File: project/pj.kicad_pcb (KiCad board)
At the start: 2 copper layers, 65 x 56.5 mm, 18 parts, among them J1 RPi_GPIO, J10 Pi PWR enable, J12 Conn_01x16_Pin, J2 2B+, J3 zero, J4 3A+, J5 3B+, J6 Pi 4, J7 Reset Pico, J8 Reset Pi, J9 Pi External PWR, SW1 Reset Pi, SW2 Reset Pico

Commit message: spi sch
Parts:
- moved J3 45.8 mm to (90.6, 48.4)
- moved J4 2.43 mm to (96.7, 52.0)
- moved J1 0.06 mm to (69.0, 44.5)
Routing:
- net Net-(A1-GPIO19): track 177.9 -> 162.9 mm
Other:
- board text added: "github.com/CarlFK/pj v1.1"
- board text removed: "github.com/CarlFK/pj v1.0"
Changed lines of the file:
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@@
 		(pad_to_mask_clearance 0)
 		(allow_soldermask_bridges_in_footprints no)
+		(grid_origin 93.15 45.89)
 		(pcbplotparams
 			(layerselection 0x00010fc_ffffffff)
@@
 		(fp_arc
 			(start 10.579676 25.189937)
-			(mid 10.357958 25.493991)
+			(mid 10.357946 25.493957)
 			(end 10 25.61)
 			(stroke
@@
 	(footprint "RPI_Hat:RPI_Hat_B+"
 		(layer "F.Cu")
-		(at 68.92 44.495)
+		(at 68.97 44.522)
 		(property "Reference" "J1"
 			(at 12.6 3.545 0)
@@
 			(layer "Dwgs.User")
 			(pts
-				(xy 41.42 60.495) (xy 36.42 60.495)
+				(xy 41.47 60.522) (xy 36.47 60.522)
 			)
 			(height 2)
-			(gr_text "5.0000 mm"
-				(at 38.92 56.845 0)
+			(gr_text "196.8504 mils"
+				(at 38.97 56.872 0)
 				(layer "Dwgs.User")
 				(effects
@@
 			(layer "Dwgs.User")
 			(pts
-				(xy 83.42 93.995) (xy 83.42 76.995)
+				(xy 83.47 94.022) (xy 83.47 77.022)
 			)
 			(height 3)
-			(gr_text "17.0000 mm"
-				(at 84.77 85.495 90)
+			(gr_text "669.2913 mils"
+				(at 84.82 85.522 90)
 				(layer "Dwgs.User")
 				(effects
@@
 			(layer "Dwgs.User")
 			(pts
-				(xy 68.92 46.495001) (xy 39.92 46.495001)
+				(xy 68.97 46.522001) (xy 39.97 46.522001)
 			)
 			(height -2.499999)
-			(gr_text "29.0000 mm"
-				(at 54.42 50.995001 0)
+			(gr_text "1141.7323 mils"
+				(at 54.47 51.022001 0)
 				(layer "Dwgs.User")
 				(effects
@@
 			(layer "Dwgs.User")
 			(pts
-				(xy 35.42 96.995) (xy 35.42 77.495)
+				(xy 35.47 97.022) (xy 35.47 77.522)
 			)
 			(height -3)
-			(gr_text "19.5000 mm"
-				(at 30.77 87.245 90)
+			(gr_text "767.7165 mils"
+				(at 30.82 87.272 90)
 				(layer "Dwgs.User")
 				(effects
@@
 			(layer "Dwgs.User")
 			(pts
-				(xy 102.42 93.495) (xy 102.42 44.495)
+				(xy 102.47 93.522) (xy 102.47 44.522)
 			)
 			(height 2.999999)
-			(gr_text "49.0000 mm"
-				(at 103.769999 68.995 90)
+			(gr_text "1929.1339 mils"
+				(at 103.819999 69.022 90)
 				(layer "Dwgs.User")
 				(effects
@@
 			(layer "Dwgs.User")
 			(pts
-				(xy 102.42 96.995) (xy 102.42 40.995)
+				(xy 102.47 97.022) (xy 102.47 41.022)
 			)
 			(height 8)
-			(gr_text "56.0000 mm"
-				(at 108.77 68.995 90)
+			(gr_text "2204.7244 mils"
+				(at 108.82 69.022 90)
 				(layer "Dwgs.User")
 				(effects
@@
 			(layer "Dwgs.User")
 			(pts
-				(xy 101.42 39.495) (xy 36.42 39.495)
+				(xy 101.47 39.522) (xy 36.47 39.522)
 			)
 			(height 7)
-			(gr_text "65.0000 mm"
-				(at 68.92 30.845 0)
+			(gr_text "2559.0551 mils"
+				(at 68.97 30.872 0)
 				(layer "Dwgs.User")
 				(effects
@@
 			(layer "Dwgs.User")
 			(pts
-				(xy 82.42 75.995) (xy 80.42 75.995)
+				(xy 82.47 76.022) (xy 80.47 76.022)
 			)
 			(height 2.499999)
-			(gr_text "2.0000 mm"
-				(at 81.42 71.845001 0)
+			(gr_text "78.7402 mils"
+				(at 81.47 71.872001 0)
 				(layer "Dwgs.User")
 				(effects
@@
 			(layer "Dwgs.User")
 			(pts
-				(xy 42.42 77.495) (xy 42.42 60.495)
+				(xy 42.47 77.522) (xy 42.47 60.522)
 			)
 			(height 2)
-			(gr_text "17.0000 mm"
-				(at 42.77 68.995 90)
+			(gr_text "669.2913 mils"
+				(at 42.82 69.022 90)
 				(layer "Dwgs.User")
 				(effects
@@
 			(layer "Dwgs.User")
 			(pts
-				(xy 102.42 96.995) (xy 102.42 40.495)
+				(xy 102.47 97.022) (xy 102.47 40.522)
 			)
 			(height 12)
-			(gr_text "56.5000 mm"
-				(at 112.77 68.745 90)
+			(gr_text "2224.4094 mils"
+				(at 112.82 68.772 90)
 				(layer "Dwgs.User")
 				(effects
@@
 			(layer "Dwgs.User")
 			(pts
-				(xy 97.92 39.495) (xy 39.92 39.495)
+				(xy 97.97 39.522) (xy 39.97 39.522)
 			)
 			(height 2.5)
-			(gr_text "58.0000 mm"
-				(at 68.92 35.345 0)
+			(gr_text "2283.4646 mils"
+				(at 68.97 35.372 0)
 				(layer "Dwgs.User")
 				(effects
@@
 			(layer "Dwgs.User")
 			(pts
-				(xy 79.42 96.995) (xy 79.42 85.495)
+				(xy 79.47 97.022) (xy 79.47 85.522)
 			)
 			(height -2.499999)
-			(gr_text "11.5000 mm"
-				(at 75.270001 91.245 90)
+			(gr_text "452.7559 mils"
+				(at 75.320001 91.272 90)
 				(layer "Dwgs.User")
 				(effects
@@
 			(layer "Dwgs.User")
 			(pts
-				(xy 39.92 97.995) (xy 36.42 97.995)
+				(xy 39.97 98.022) (xy 36.47 98.022)
 			)
 			(height -2.5)
-			(gr_text "3.5000 mm"
-				(at 38.17 98.845 0)
+			(gr_text "137.7953 mils"
+				(at 38.22 98.872 0)
 				(layer "Dwgs.User")
 				(effects
@@
 			(layer "Dwgs.User")
 			(pts
-				(xy 43.42 96.995) (xy 43.42 93.495)
+				(xy 43.47 97.022) (xy 43.47 93.522)
 			)
 			(height 3)
-			(gr_text "3.5000 mm"
-				(at 44.77 95.245 90)
+			(gr_text "137.7953 mils"
+				(at 44.82 95.272 90)
 				(layer "Dwgs.User")
 				(effects
@@
 	(footprint "Connector_PinSocket_2.54mm:PinSocket_1x02_P2.54mm_Vertical"
 		(layer "B.Cu")
-		(at 44.82 48.37 -90)
+		(at 90.61 48.43 -90)
 		(descr "Through hole straight socket strip, 1x02, 2.54mm pitch, single row (from Kicad 4.0.7), script generated")
 		(tags "Through hole socket strip THT 1x02 2.54mm single row")
@@
 		)
 		(property "Value" "zero"
-			(at 0.76 2.76 0)
+			(at 0 -5.08 0)
 			(layer "F.SilkS")
 			(effects
@@
 	(footprint "Connector_PinSocket_2.54mm:PinSocket_1x02_P2.54mm_Vertical"
 		(layer "B.Cu")
-		(at 96.69 49.61 -90)
+		(at 96.72 52.04 -90)
 		(descr "Through hole straight socket strip, 1x02, 2.54mm pitch, single row (from Kicad 4.0.7), script generated")
 		(tags "Through hole socket strip THT 1x02 2.54mm single row")
@@
 		)
 		(property "Value" "3A+"
-			(at 2.09 -0.41 180)
+			(at -1.86 -0.19 180)
 			(layer "F.SilkS")
 			(effects
@@
 		)
 	)
-	(gr_text "github.com/CarlFK/pj v1.0"
+	(gr_text "github.com/CarlFK/pj v1.1"
+		(locked yes)
 		(at 97.55 59.4 270)
 		(layer "F.SilkS")
@@
 	)
 	(segment
-		(start 41.23 54.26)
-		(end 41.23 55.92)
+		(start 99.21 57.08)
+		(end 99.22 57.09)
 		(width 0.2)
 		(layer "F.Cu")
@@
 	)
 	(segment
-		(start 39.92 49.06)
-		(end 39.92 52.95)
-		(width 0.2)
-		(layer "F.Cu")
-		(net 13)
-	)
-	(segment
-		(start 44.82 48.37)
-		(end 40.61 48.37)
-		(width 0.2)
-		(layer "F.Cu")
-		(net 13)
-	)
-	(segment
-		(start 96.69 52.13)
-		(end 99.22 54.66)
+		(start 96.72 52.04)
+		(end 96.72 53.26)
 		(width 0.2)
 		(layer "F.Cu")
@@
 	)
 	(segment
-		(start 40.61 48.37)
-		(end 39.92 49.06)
-		(width 0.2)
-		(layer "F.Cu")
-		(net 13)
-	)
-	(segment
 		(start 99.22 57.09)
 		(end 99.22 67.51)
@@
 	)
 	(segment
-		(start 99.22 57.09)
-		(end 99.22 54.66)
+		(start 48.32 80.83)
+		(end 46 78.51)
 		(width 0.2)
 		(layer "F.Cu")
@@
 	)
 	(segment
-		(start 48.32 80.83)
-		(end 46 78.51)
+		(start 96.72 53.26)
+		(end 99.21 55.75)
 		(width 0.2)
 		(layer "F.Cu")
@@
 	)
 	(segment
+		(start 99.21 55.75)
+		(end 99.21 57.08)
+		(width 0.2)
+		(layer "F.Cu")
+		(net 13)
+	)
+	(segment
 		(start 54.91 71.3425)
 		(end 54.8475 71.28)
@@
 	)
 	(segment
-		(start 39.92 52.95)
-		(end 41.23 54.26)
-		(width 0.2)
-		(layer "F.Cu")
-		(net 13)
-	)
-	(segment
 		(start 44.075 76.585)
 		(end 46 78.51)
@@
 		(width 0.2)
 		(layer "F.Cu")
-		(net 13)
-	)
-	(segment
-		(start 96.69 49.61)
-		(end 96.69 52.13)
-		(width 0.2)
-		(layer "F.Cu")

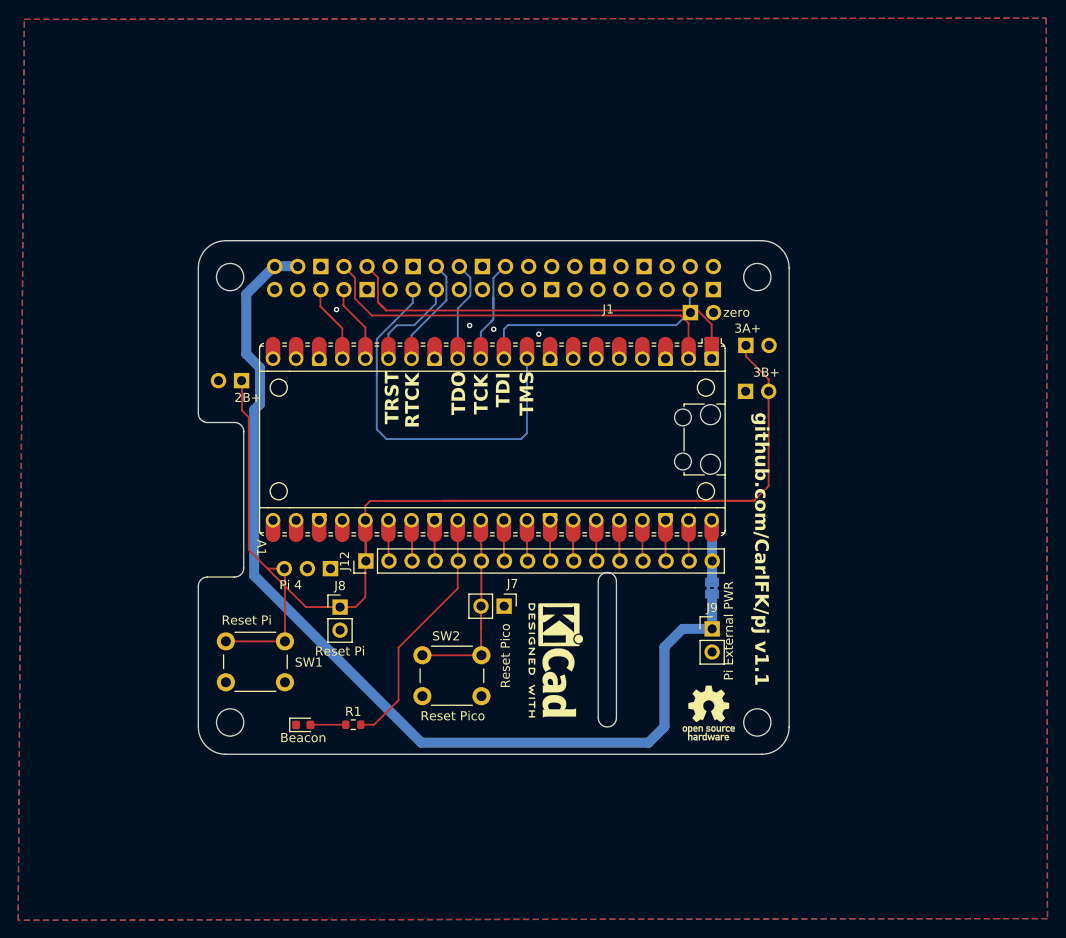
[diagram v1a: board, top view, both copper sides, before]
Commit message: add spi symbol
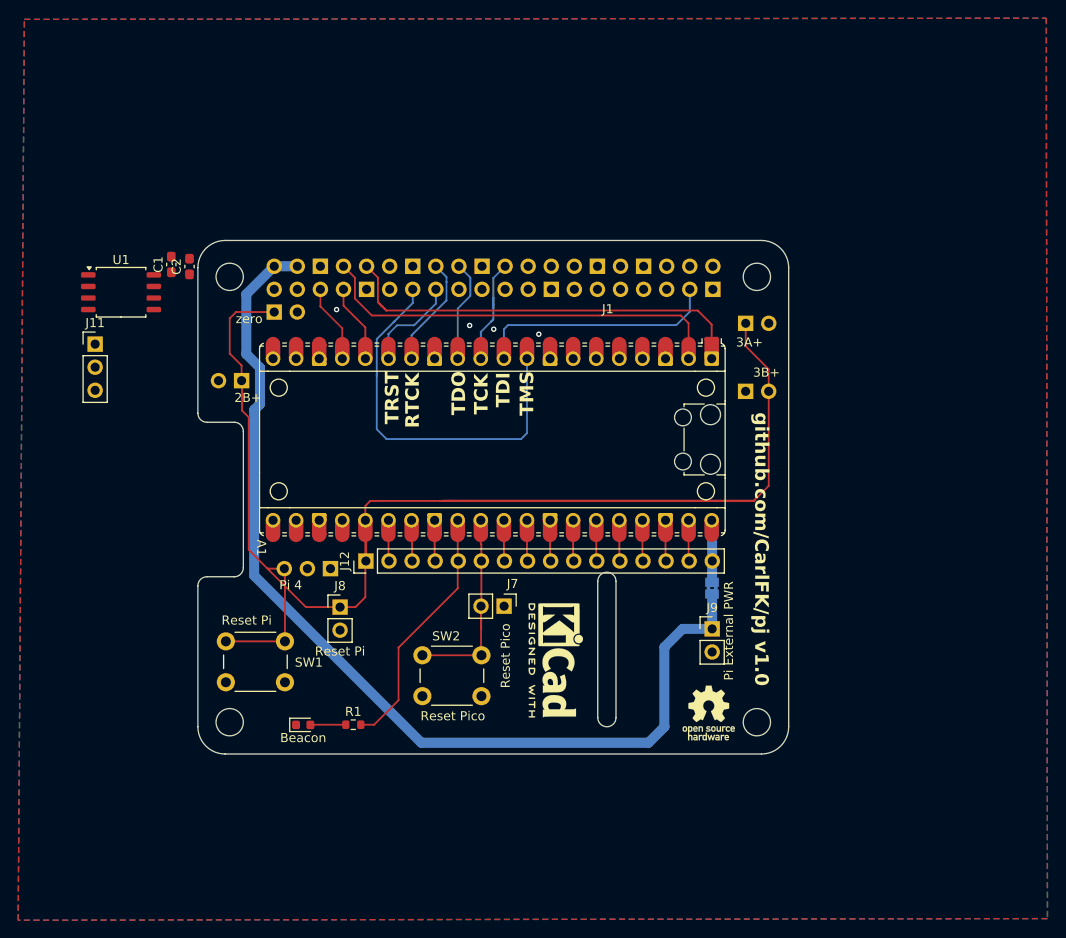
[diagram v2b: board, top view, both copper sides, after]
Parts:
- added C1: .1, Capacitor_SMD:C_0603_1608Metric_Pad1.08x0.95mm_HandSolder, F.Cu at (33.5, 43.1)
- added C2: 1, Capacitor_SMD:C_0603_1608Metric_Pad1.08x0.95mm_HandSolder, F.Cu at (35.5, 43.4)
- added J11: Conn_01x03_Pin, Connector_PinHeader_2.54mm:PinHeader_1x03_P2.54mm_Vertical, F.Cu at (25.1, 51.9)
- added U1: W25Q32JVSS, Package_SO:SOIC-8_5.23x5.23mm_P1.27mm, F.Cu at (28.0, 46.2)
- moved J3 45.8 mm to (44.8, 48.4)
- moved J4 2.43 mm to (96.7, 49.6)
- moved J1 0.06 mm to (68.9, 44.5)
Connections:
- net Net-(A1-3V3) renamed +3.3V
- net Net-(A1-GPIO19) renamed /reset pi
- net Net-(A1-VBUS) renamed /pi power
- A1 pad 19: unconnected-(A1-GPIO14-Pad19) -> /RPI_SPI_CE0
- A1 pad 20: unconnected-(A1-GPIO15-Pad20) -> /RPI_SPI_CE1
- A1 pad 4: unconnected-(A1-GPIO2-Pad4) -> /RPI_SPI_CLK
- A1 pad 5: unconnected-(A1-GPIO3-Pad5) -> /RPI_SPI_MISO
- A1 pad 6: unconnected-(A1-GPIO4-Pad6) -> /RPI_SPI_MOSI
- J1 pad 19: unconnected-(J1-BCM10_MOSI-Pad19) -> /RPI_SPI_MOSI
- J1 pad 21: unconnected-(J1-BCM9_MISO-Pad21) -> /RPI_SPI_MISO
- J1 pad 23: unconnected-(J1-BCM11_SCLK-Pad23) -> /RPI_SPI_CLK
- J1 pad 24: unconnected-(J1-BCM8_CE0-Pad24) -> /RPI_SPI_CE0
- J1 pad 26: unconnected-(J1-BCM7_CE1-Pad26) -> /RPI_SPI_CE1
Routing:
- net /reset pi: track 162.9 -> 177.9 mm
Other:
- board text added: "github.com/CarlFK/pj v1.0"
- board text removed: "github.com/CarlFK/pj v1.1"

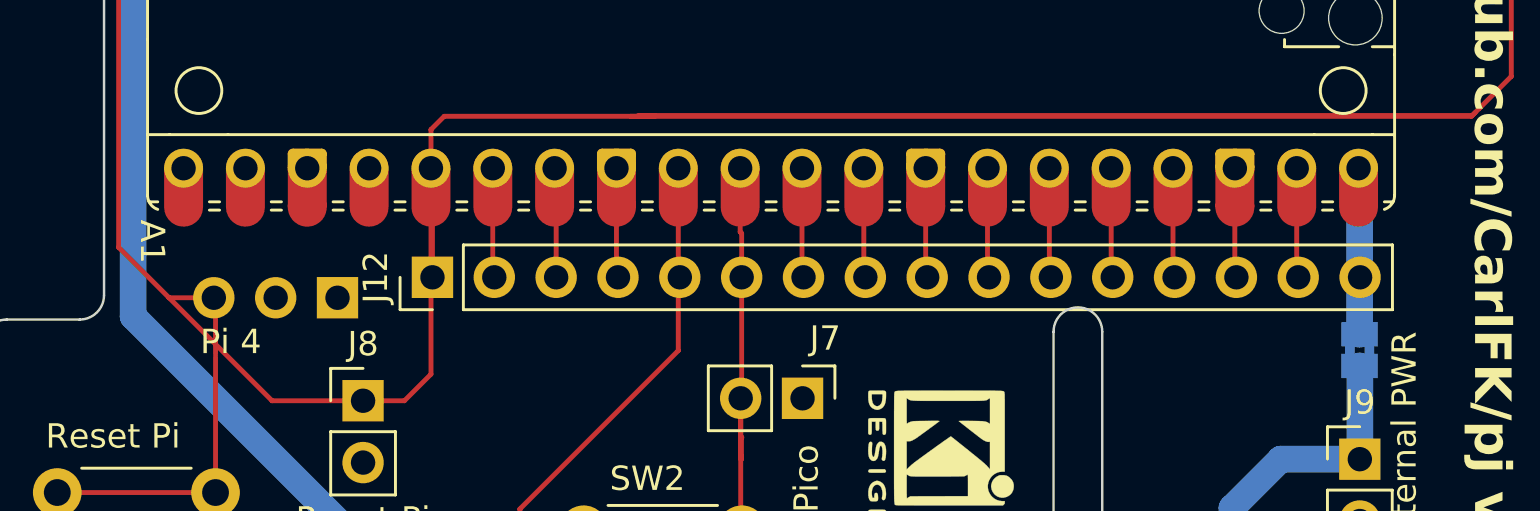
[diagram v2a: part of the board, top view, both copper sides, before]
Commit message: removing debug header
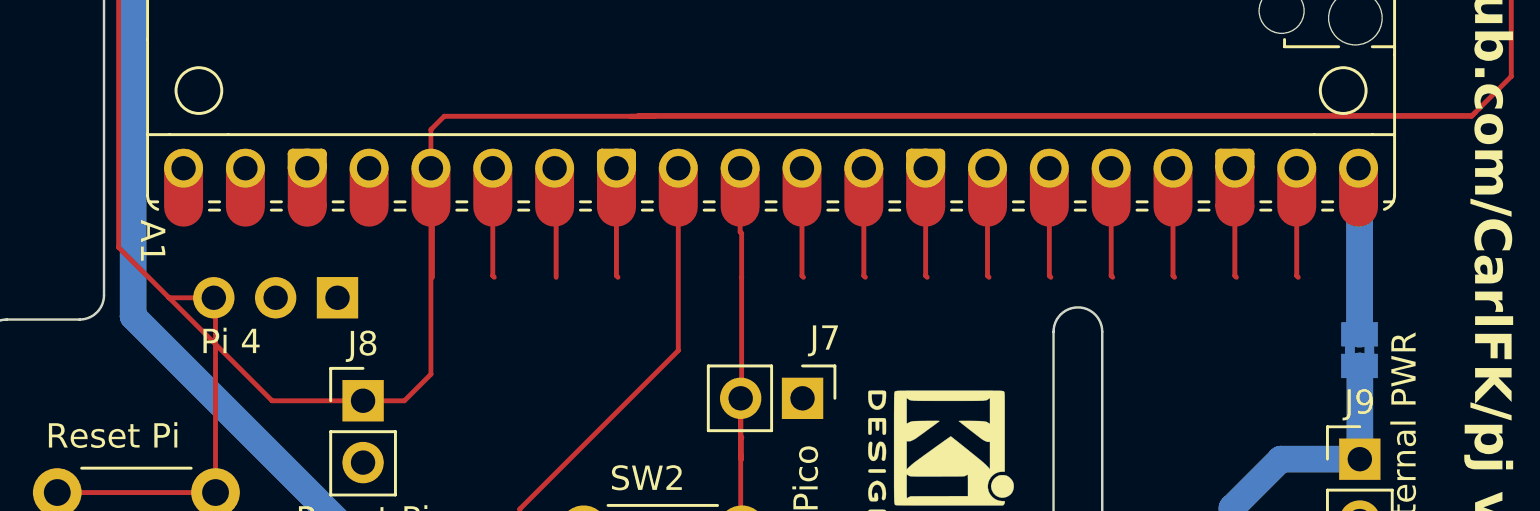
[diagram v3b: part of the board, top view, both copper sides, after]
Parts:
- removed J12: Conn_01x16_Pin, Connector_PinHeader_2.54mm:PinHeader_1x16_P2.54mm_Vertical
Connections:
- A1 pad 26: Net-(A1-GPIO20) -> unconnected-(A1-GPIO20-Pad26)
- A1 pad 27: Net-(A1-GPIO21) -> unconnected-(A1-GPIO21-Pad27)
- A1 pad 31: Net-(A1-GPIO26_ADC0) -> unconnected-(A1-GPIO26_ADC0-Pad31)
- A1 pad 32: Net-(A1-GPIO27_ADC1) -> unconnected-(A1-GPIO27_ADC1-Pad32)
- A1 pad 33: Net-(A1-AGND) -> unconnected-(A1-AGND-Pad33)
- A1 pad 34: Net-(A1-GPIO28_ADC2) -> unconnected-(A1-GPIO28_ADC2-Pad34)
- A1 pad 35: Net-(A1-ADC_VREF) -> unconnected-(A1-ADC_VREF-Pad35)
- A1 pad 37: Net-(A1-3V3_EN) -> unconnected-(A1-3V3_EN-Pad37)
- A1 pad 39: Net-(A1-VSYS) -> unconnected-(A1-VSYS-Pad39)
- J7 pad 1: unconnected-(J7-Pin_1-Pad1) -> GND
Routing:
- net unconnected-(A1-GPIO20-Pad26): track 0.00 -> 4.52 mm
- net Net-(A1-GPIO20): track 4.52 -> 0.00 mm
- net unconnected-(A1-VSYS-Pad39): track 0.00 -> 4.51 mm
- net unconnected-(A1-GPIO28_ADC2-Pad34): track 0.00 -> 4.51 mm
- net unconnected-(A1-GPIO27_ADC1-Pad32): track 0.00 -> 4.51 mm
- net unconnected-(A1-GPIO26_ADC0-Pad31): track 0.00 -> 4.51 mm
- net unconnected-(A1-GPIO21-Pad27): track 0.00 -> 4.51 mm
- net unconnected-(A1-AGND-Pad33): track 0.00 -> 4.51 mm
- net unconnected-(A1-ADC_VREF-Pad35): track 0.00 -> 4.51 mm
- net unconnected-(A1-3V3_EN-Pad37): track 0.00 -> 4.51 mm
- net Net-(A1-VSYS): track 4.51 -> 0.00 mm
- net Net-(A1-GPIO28_ADC2): track 4.51 -> 0.00 mm
- net Net-(A1-GPIO27_ADC1): track 4.51 -> 0.00 mm
- net Net-(A1-GPIO26_ADC0): track 4.51 -> 0.00 mm
- net Net-(A1-GPIO21): track 4.51 -> 0.00 mm
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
